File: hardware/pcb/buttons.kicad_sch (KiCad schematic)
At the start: 7 parts, among them SW1 SW_Push, SW2 SW_Push, SW3 SW_Push, SW4 SW_Push, SW5 SW_Push

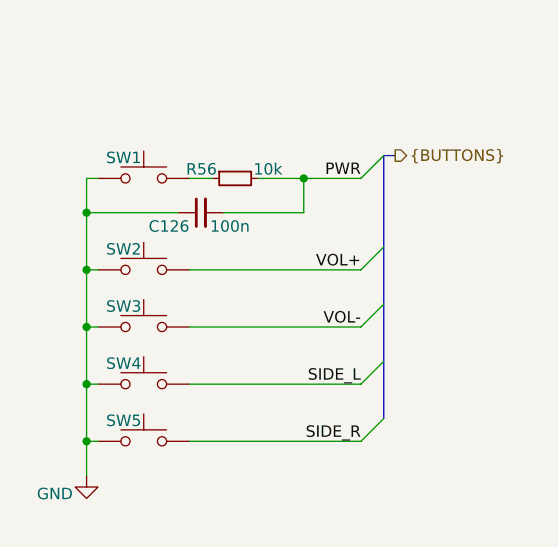
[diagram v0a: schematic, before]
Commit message: fixed small issues with footprint pad names
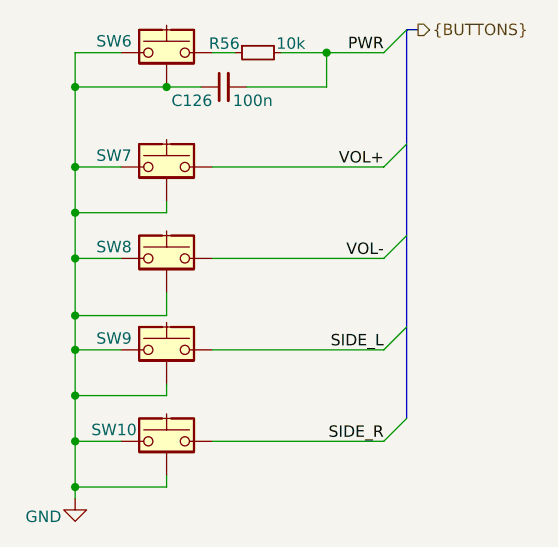
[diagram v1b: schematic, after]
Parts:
- removed SW1, SW2, SW3, SW4, SW5: SW_Push, Button_Switch_SMD:SW_Push_1P1T-MP_NO_Horizontal_Alps_SKRTLAE010, symbol Switch:SW_Push
- added SW10, SW6, SW7, SW8, SW9: SW_Push_Shielded, Button_Switch_SMD:SW_Push_1P1T-MP_NO_Horizontal_Alps_SKRTLAE010, symbol Switch:SW_Push_Shielded
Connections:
- net GND: now also SW10.1, SW10.MP (B), SW6.1, SW6.MP (B), SW7.1, SW7.MP (B), SW8.1, SW8.MP (B), SW9.1, SW9.MP (B)
- net SIDE_L: now also SW9.2
- net SIDE_R: now also SW10.2
- net VOL+: now also SW7.2
- net VOL-: now also SW8.2
- net at R56.1: now also SW6.2
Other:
- moved on the sheet: C126, R56

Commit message: moved some caps to 0201
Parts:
- C126: footprint Capacitor_SMD:C_0402_1005Metric -> Capacitor_SMD:C_0201_0603Metric
- renumbered SW6 to SW1, SW7 to SW2, SW8 to SW3, SW9 to SW4, SW10 to SW5
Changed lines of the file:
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@@
 		(in_pos_files yes)
 		(dnp no)
-		(property "Reference" "SW10"
+		(property "Reference" "SW5"
 			(at 85.598 80.01 0)
 			(show_name no)
@@
 			(project "meko"
 				(path "/da54f10a-146b-4941-a9c7-55c7173bb101/e40fc879-1a0f-4948-9e1c-6c4ee1733e71"
-					(reference "SW10")
+					(reference "SW5")
 					(unit 1)
 				)
@@
 		(in_pos_files yes)
 		(dnp no)
-		(property "Reference" "SW7"
+		(property "Reference" "SW2"
 			(at 85.598 49.53 0)
 			(show_name no)
@@
 			(project "meko"
 				(path "/da54f10a-146b-4941-a9c7-55c7173bb101/e40fc879-1a0f-4948-9e1c-6c4ee1733e71"
-					(reference "SW7")
+					(reference "SW2")
 					(unit 1)
 				)
@@
 		(in_pos_files yes)
 		(dnp no)
-		(property "Reference" "SW9"
+		(property "Reference" "SW4"
 			(at 85.598 69.85 0)
 			(show_name no)
@@
 			(project "meko"
 				(path "/da54f10a-146b-4941-a9c7-55c7173bb101/e40fc879-1a0f-4948-9e1c-6c4ee1733e71"
-					(reference "SW9")
+					(reference "SW4")
 					(unit 1)
 				)
@@
 		(in_pos_files yes)
 		(dnp no)
-		(property "Reference" "SW6"
+		(property "Reference" "SW1"
 			(at 85.598 36.83 0)
 			(show_name no)
@@
 			(project "meko"
 				(path "/da54f10a-146b-4941-a9c7-55c7173bb101/e40fc879-1a0f-4948-9e1c-6c4ee1733e71"
-					(reference "SW6")
+					(reference "SW1")
 					(unit 1)
 				)
@@
 			)
 		)
-		(property "Footprint" "Capacitor_SMD:C_0402_1005Metric"
+		(property "Footprint" "Capacitor_SMD:C_0201_0603Metric"
 			(at 97.79 41.91 0)
 			(hide yes)
@@
 		(in_pos_files yes)
 		(dnp no)
-		(property "Reference" "#PWR0141"
+		(property "Reference" "#PWR0142"
 			(at 81.28 93.98 0)
 			(hide yes)
@@
 			(project "meko"
 				(path "/da54f10a-146b-4941-a9c7-55c7173bb101/e40fc879-1a0f-4948-9e1c-6c4ee1733e71"
-					(reference "#PWR0141")
+					(reference "#PWR0142")
 					(unit 1)
 				)
@@
 		(in_pos_files yes)
 		(dnp no)
-		(property "Reference" "SW8"
+		(property "Reference" "SW3"
 			(at 85.598 59.69 0)
 			(show_name no)
@@
 			(project "meko"
 				(path "/da54f10a-146b-4941-a9c7-55c7173bb101/e40fc879-1a0f-4948-9e1c-6c4ee1733e71"
-					(reference "SW8")
+					(reference "SW3")
 					(unit 1)
 				)
